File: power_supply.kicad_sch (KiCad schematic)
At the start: 7 parts, among them Q2 2N7002, T2 Transformer_SP_2S

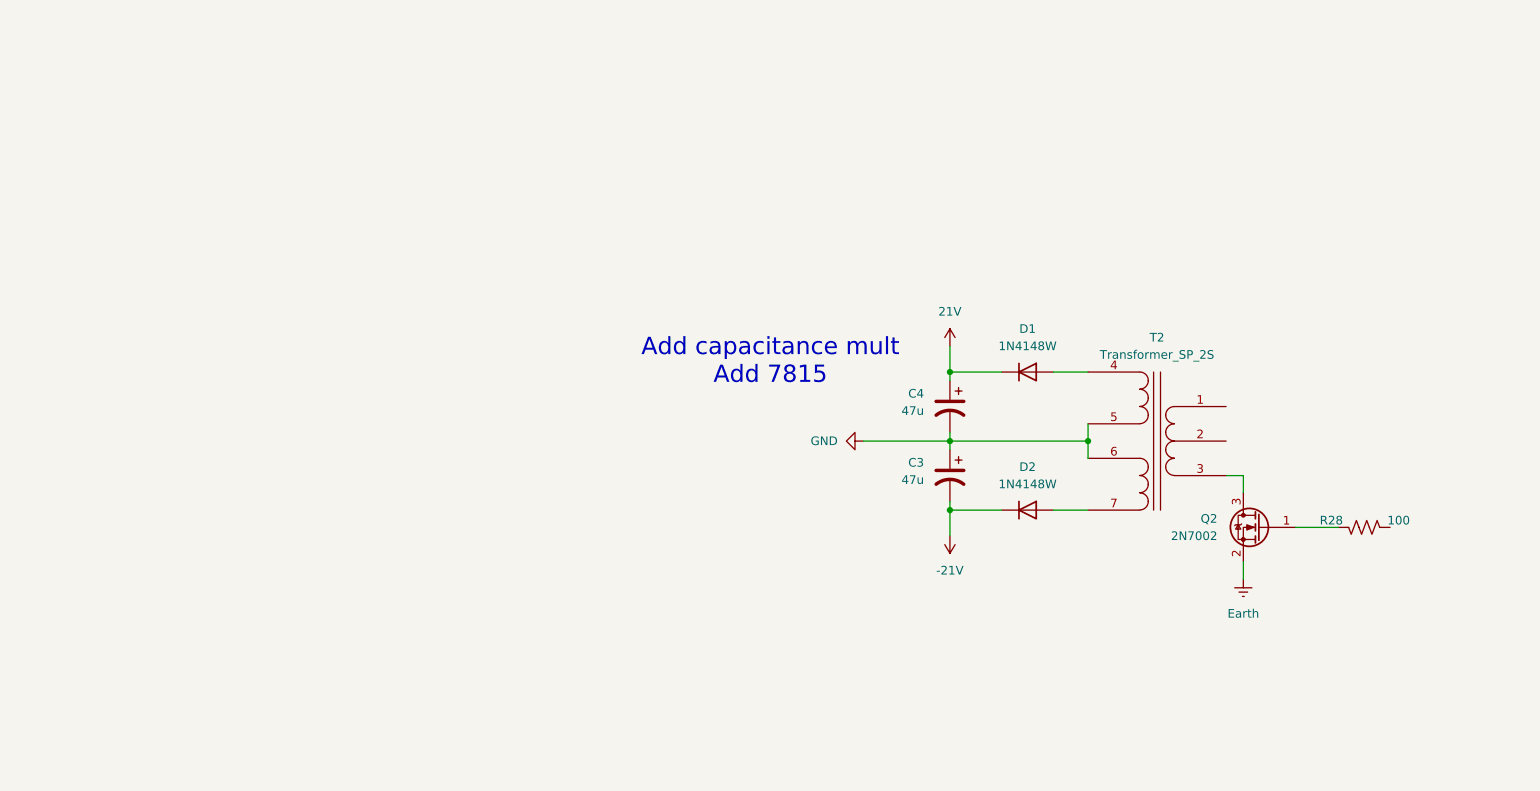
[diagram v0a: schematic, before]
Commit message: Bootstraped input buffer.
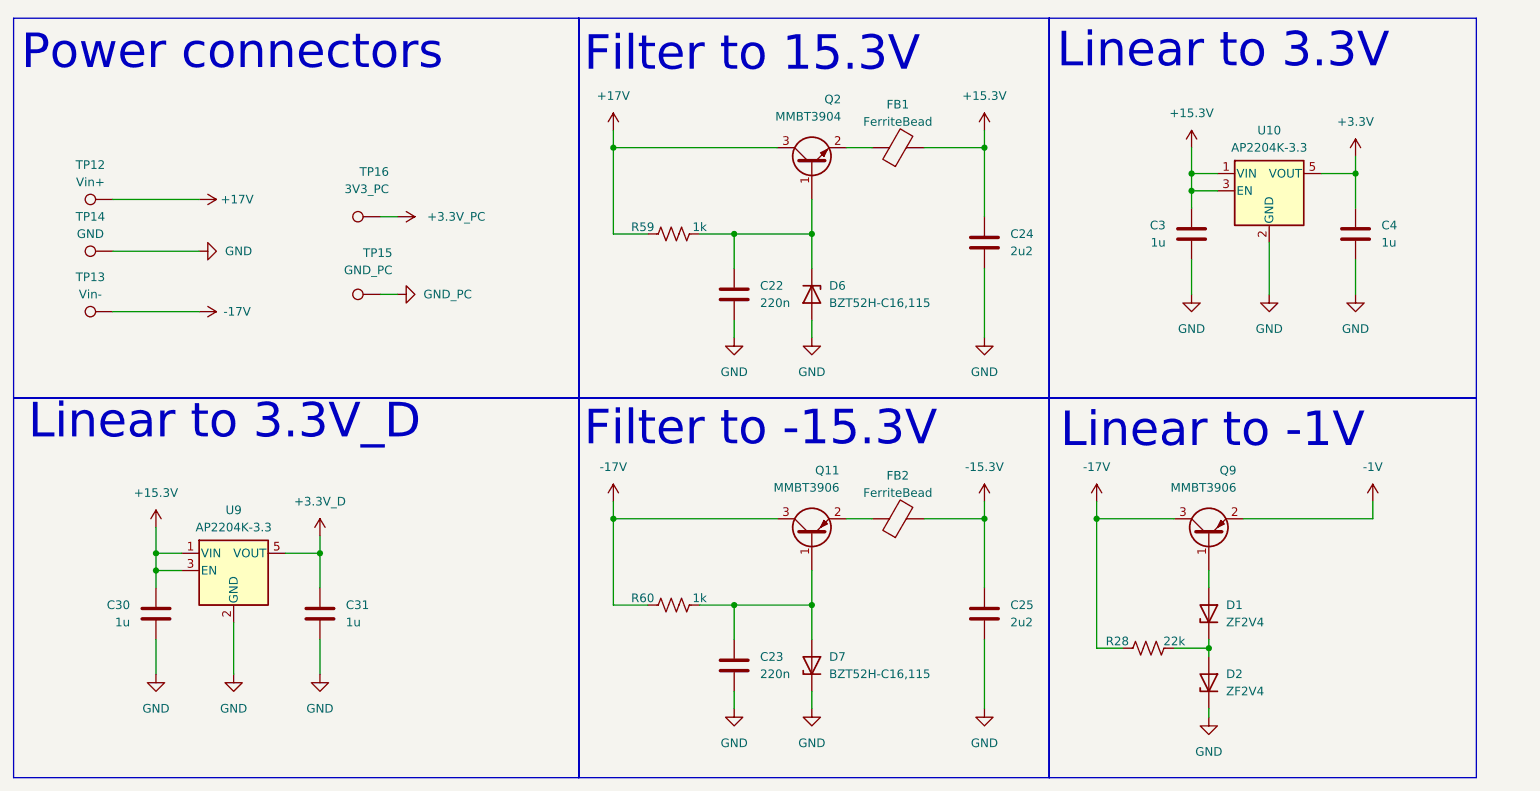
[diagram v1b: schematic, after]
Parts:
- removed C3, C4: 47u, Capacitor_THT:CP_Radial_D5.0mm_P2.00mm, symbol Device:C_Polarized_US
- removed D1, D2: 1N4148W, Diode_SMD:D_SOD-123, symbol Diode:1N4148W
- removed Q2: 2N7002, Package_TO_SOT_SMD:SOT-23, symbol Transistor_FET:2N7002
- removed T2: Transformer_SP_2S, symbol Device:Transformer_SP_2S
- added C22, C23: 220n, Resistor_SMD:R_0603_1608Metric_Pad0.98x0.95mm_HandSolder, symbol Device:C
- added C24, C25: 2u2, Resistor_SMD:R_1206_3216Metric_Pad1.30x1.75mm_HandSolder, symbol Device:C
- added C3, C30, C31, C4: 1u, Resistor_SMD:R_0603_1608Metric_Pad0.98x0.95mm_HandSolder, symbol Device:C
- added D1, D2: ZF2V4, Diode_THT:D_DO-35_SOD27_P7.62mm_Horizontal, symbol Diode:BZV55B2V4
- added D6, D7: BZT52H-C16,115, Diode_SMD:D_SOD-123F, symbol Diode:BZV55C62
- added FB1, FB2: FerriteBead, symbol Device:FerriteBead
- added Q11, Q9: MMBT3906, Package_TO_SOT_SMD:SOT-23, symbol Transistor_BJT:MMBT3906
- added Q2: MMBT3904, Package_TO_SOT_SMD:SOT-23, symbol Transistor_BJT:MMBT3904
- added R59, R60: 1k, Resistor_SMD:R_0603_1608Metric_Pad0.98x0.95mm_HandSolder, symbol Device:R_US
- added TP12: Vin+, TestPoint:TestPoint_THTPad_D4.0mm_Drill2.0mm, symbol Connector:TestPoint
- added TP13: Vin-, TestPoint:TestPoint_THTPad_D4.0mm_Drill2.0mm, symbol Connector:TestPoint
- added TP14: GND, TestPoint:TestPoint_THTPad_D4.0mm_Drill2.0mm, symbol Connector:TestPoint
- added TP15: GND_PC, TestPoint:TestPoint_THTPad_D4.0mm_Drill2.0mm, symbol Connector:TestPoint
- added TP16: 3V3_PC, TestPoint:TestPoint_THTPad_D4.0mm_Drill2.0mm, symbol Connector:TestPoint
- added U10, U9: AP2204K-3.3, Package_TO_SOT_SMD:SOT-23-5, symbol Regulator_Linear:AP2204K-3.3
- R28: value 100 -> 22k
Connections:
- net GND: now also C22.2, C23.2, C24.1, C25.1, C3.2, C30.2, C31.2, C4.2, D2.1 (K), D6.2 (A), D7.1 (K), TP14.1, U10.2 (GND), U9.2 (GND)
- net -17V: now reaches R28.2
- net -17V: now also Q11.3 (C), Q9.3 (C), R60.2, TP13.1
- net at R28.1: now also D1.1 (K), D2.2 (A)
- new net: C23.1, D7.2 (A), Q11.1 (B), R60.1
- new net: FB2.1, Q11.2 (E)
- new net: C22.1, D6.1 (K), Q2.1 (B), R59.1
- new net: FB1.1, Q2.2 (E)
- new net: D1.2 (A), Q9.1 (B)
- new net +15.3V: C24.2, C3.1, C30.1, FB1.2, U10.1 (VIN), U10.3 (EN), U9.1 (VIN), U9.3 (EN)
- new net +17V: Q2.3 (C), R59.2, TP12.1
- new net +3.3V: C4.1, U10.5 (VOUT)
- new net +3.3V_D: C31.1, U9.5 (VOUT)
- new net +3.3V_PC: TP16.1
- new net -15.3V: C25.2, FB2.2
- new net -1V: Q9.2 (E)
- new net GND_PC: TP15.1
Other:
- note added: "Filter to -15.3V"
- note added: "Filter to 15.3V"
- note added: "Linear to -1V"
- note added: "Linear to 3.3V"
- note added: "Linear to 3.3V_D"
- note added: "Power connectors"
- note removed: "Add capacitance mult Add 7815"
